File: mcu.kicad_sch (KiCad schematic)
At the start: 29 parts, among them J1 SM03B-SRSS-TB, SW1 SW_Push, SW2 SW_Push, U1 RP2350_60QFN, U2 W25Q128JVS, Y1 ABM8-272-T3

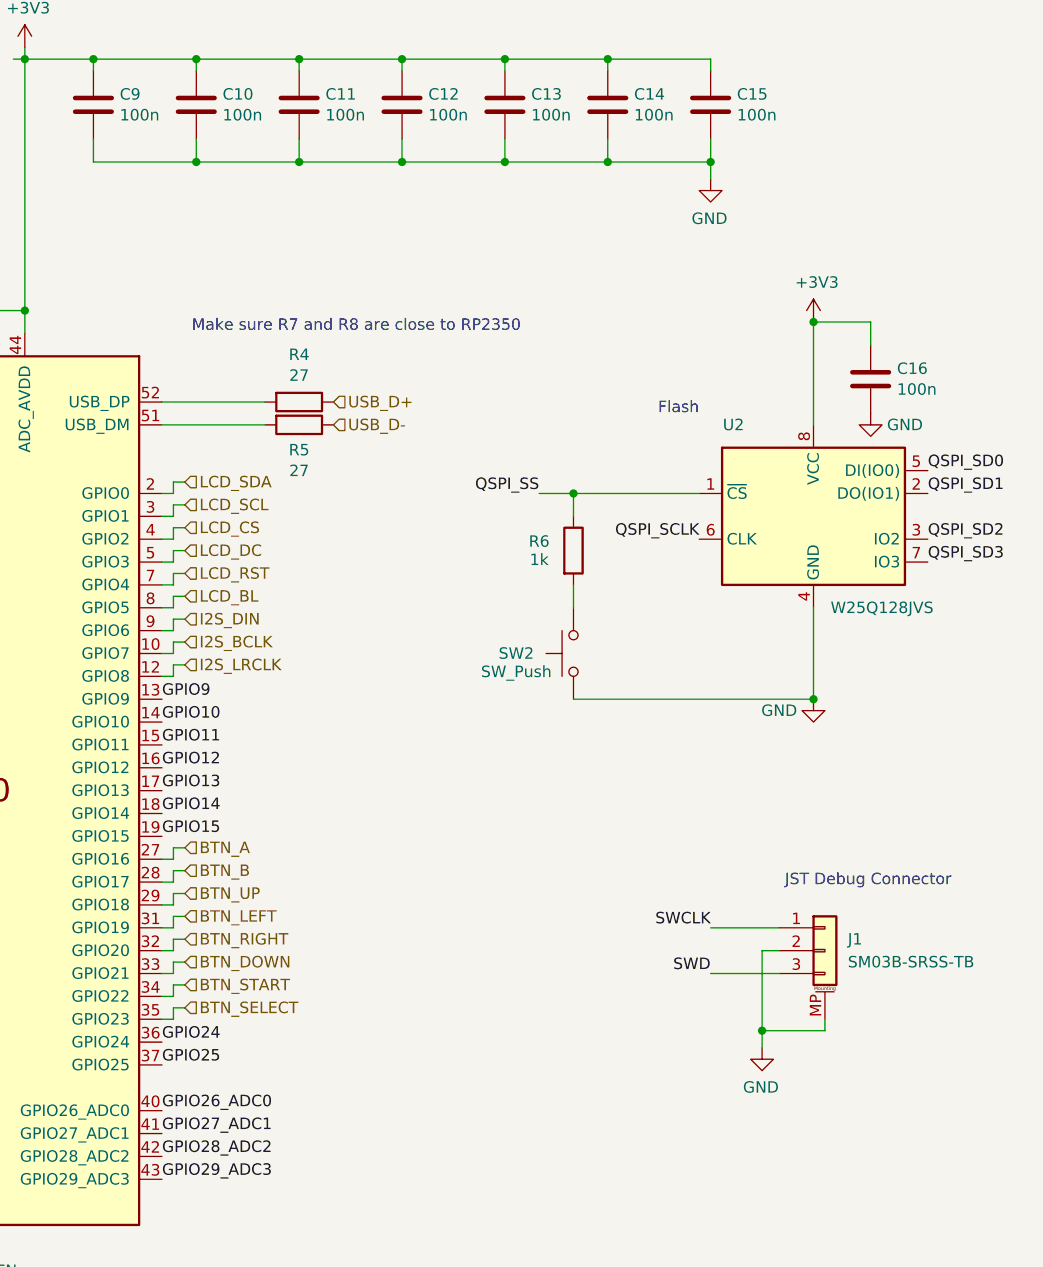
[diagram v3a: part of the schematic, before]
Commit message: add amplifier mode selector, add drawing lcd
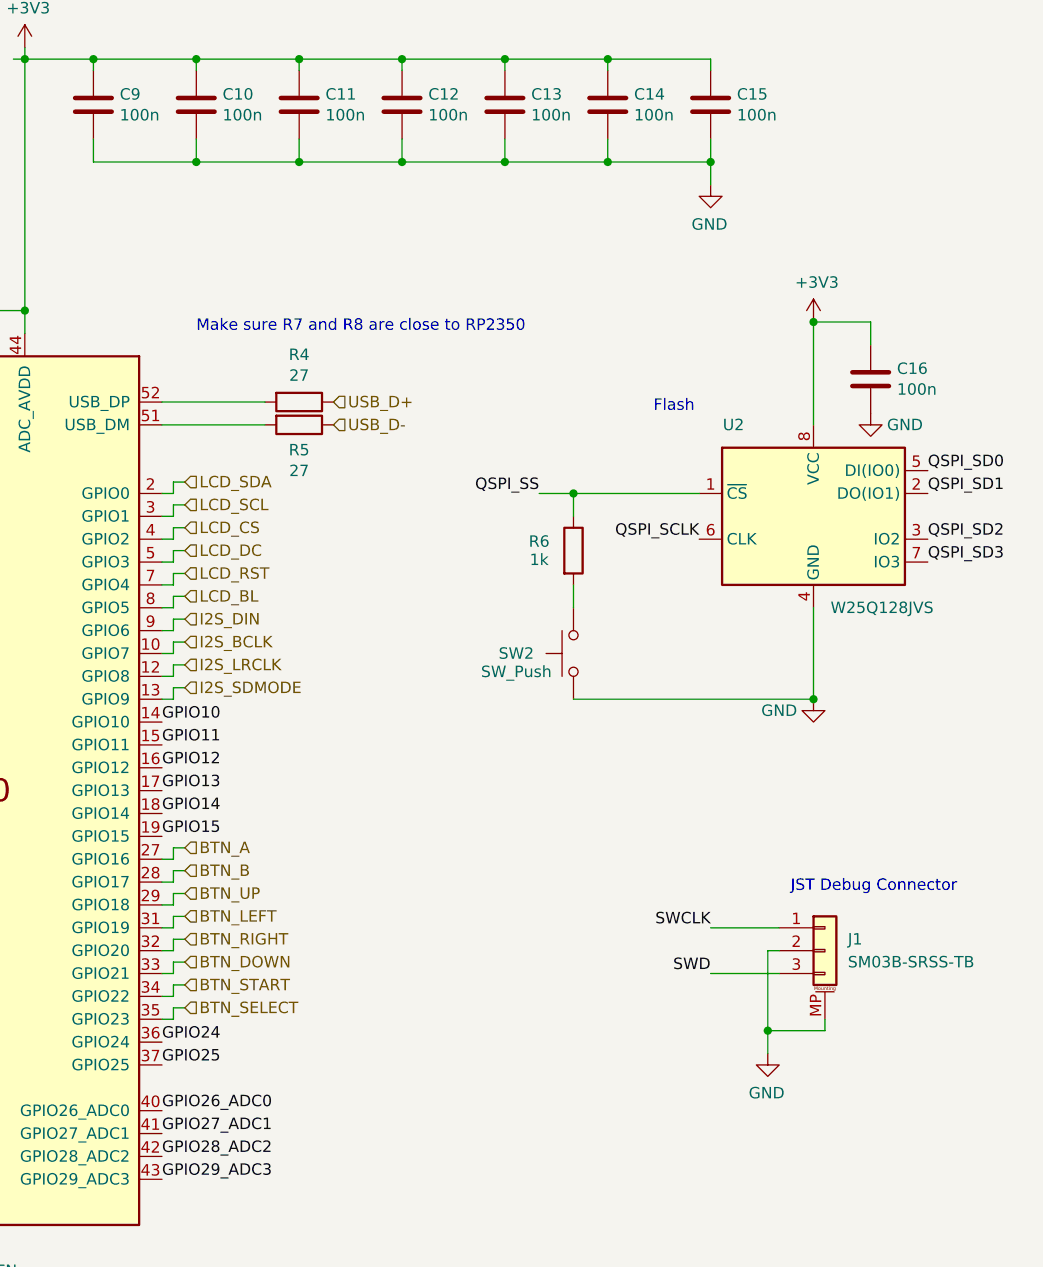
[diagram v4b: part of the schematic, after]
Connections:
- net GPIO9 renamed I2S_SDMODE
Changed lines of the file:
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@@
 	(text "Make sure R7 and R8 are close to RP2350\n"
 		(exclude_from_sim no)
-		(at 178.562 60.96 0)
+		(at 179.07 60.96 0)
 		(effects
 			(font
@@
 	(text "Flash"
 		(exclude_from_sim no)
-		(at 230.378 70.104 0)
+		(at 229.87 69.85 0)
 		(effects
 			(font
@@
 	(text "JST Debug Connector"
 		(exclude_from_sim no)
-		(at 244.475 122.555 0)
+		(at 245.11 123.19 0)
 		(effects
 			(font
@@
 	)
 	(junction
-		(at 241.935 138.43)
+		(at 242.57 138.43)
 		(diameter 0)
 		(color 0 0 0 0)
@@
 	(wire
 		(pts
-			(xy 236.22 41.91) (xy 236.22 43.815)
+			(xy 236.22 41.91) (xy 236.22 44.45)
 		)
 		(stroke
@@
 	(wire
 		(pts
+			(xy 176.53 101.6) (xy 175.26 101.6)
+		)
+		(stroke
+			(width 0)
+			(type default)
+		)
+	)
+	(wire
+		(pts
 			(xy 68.58 120.65) (xy 68.58 121.92)
 		)
@@
 	(wire
 		(pts
-			(xy 241.935 138.43) (xy 241.935 140.335)
+			(xy 176.53 100.33) (xy 176.53 101.6)
+		)
+		(stroke
+			(width 0)
+			(type default)
+		)
+	)
+	(wire
+		(pts
+			(xy 242.57 138.43) (xy 242.57 140.97)
 		)
 		(stroke
@@
 	(wire
 		(pts
-			(xy 241.935 138.43) (xy 248.92 138.43)
+			(xy 242.57 138.43) (xy 248.92 138.43)
 		)
 		(stroke
@@
 	(wire
 		(pts
+			(xy 176.53 100.33) (xy 177.8 100.33)
+		)
+		(stroke
+			(width 0)
+			(type default)
+		)
+	)
+	(wire
+		(pts
 			(xy 46.99 121.92) (xy 46.99 124.46)
 		)
@@
 	(wire
 		(pts
-			(xy 243.84 129.54) (xy 241.935 129.54)
+			(xy 243.84 129.54) (xy 242.57 129.54)
 		)
 		(stroke
@@
 	(wire
 		(pts
-			(xy 241.935 129.54) (xy 241.935 138.43)
+			(xy 242.57 129.54) (xy 242.57 138.43)
 		)
 		(stroke
@@
 		)
 	)
-	(label "GPIO9"
-		(at 175.26 101.6 0)
-		(effects
-			(font
-				(size 1.27 1.27)
-			)
-			(justify left bottom)
-		)
-	)
 	(label "QSPI_SD3"
 		(at 111.76 101.6 180)
@@
 		)
 	)
+	(hierarchical_label "I2S_SDMODE"
+		(shape input)
+		(at 177.8 100.33 0)
+		(effects
+			(font
+				(size 1.27 1.27)
+			)
+			(justify left)
+		)
+	)
 	(hierarchical_label "BTN_START"
 		(shape input)
@@
 	(symbol
 		(lib_id "power:GND")
-		(at 241.935 140.335 0)
+		(at 242.57 140.97 0)
 		(mirror y)
 		(unit 1)
@@
 		(dnp no)
 		(property "Reference" "#PWR014"
-			(at 241.935 146.685 0)
+			(at 242.57 147.32 0)
 			(effects
 				(font
@@
 		)
 		(property "Value" "GND"
-			(at 241.808 144.7292 0)
+			(at 242.443 145.3642 0)
 			(effects
 				(font
@@
 		)
 		(property "Footprint" ""
-			(at 241.935 140.335 0)
+			(at 242.57 140.97 0)
 			(effects
 				(font
@@
 		)
 		(property "Datasheet" ""
-			(at 241.935 140.335 0)
+			(at 242.57 140.97 0)
 			(effects
 				(font
@@
 		)
 		(property "Description" ""
-			(at 241.935 140.335 0)
+			(at 242.57 140.97 0)
 			(effects
 				(font
@@
 	(symbol
 		(lib_id "power:GND")
-		(at 236.22 43.815 0)
+		(at 236.22 44.45 0)
 		(mirror y)
 		(unit 1)
@@
 		(dnp no)
 		(property "Reference" "#PWR013"
-			(at 236.22 50.165 0)
+			(at 236.22 50.8 0)
 			(effects
 				(font
@@
 		)
 		(property "Value" "GND"
-			(at 236.093 48.2092 0)
+			(at 236.093 48.8442 0)
 			(effects
 				(font
@@
 		)
 		(property "Footprint" ""
-			(at 236.22 43.815 0)
+			(at 236.22 44.45 0)
 			(effects
 				(font
@@
 		)
 		(property "Datasheet" ""
-			(at 236.22 43.815 0)
+			(at 236.22 44.45 0)
 			(effects
 				(font
@@
 		)
 		(property "Description" ""
-			(at 236.22 43.815 0)
+			(at 236.22 44.45 0)
 			(effects
 				(font

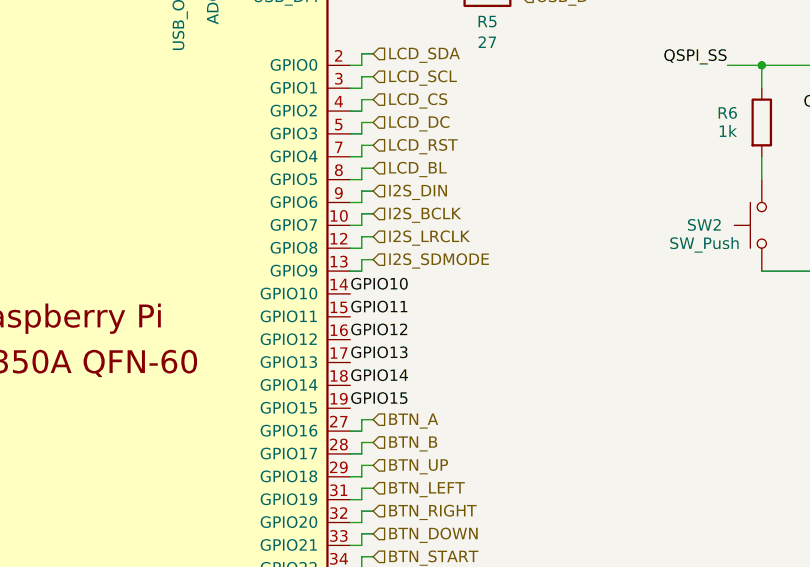
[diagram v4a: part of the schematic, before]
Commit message: add vibration motor
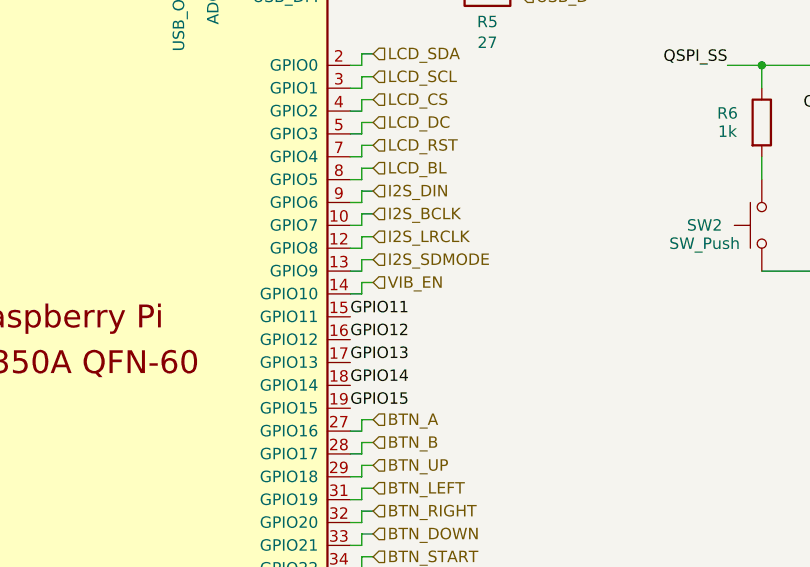
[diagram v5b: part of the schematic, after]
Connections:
- net GPIO10 renamed VIB_EN
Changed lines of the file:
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@@
+	(wire
+		(pts
+			(xy 176.53 104.14) (xy 175.26 104.14)
+		)
+		(stroke
+			(width 0)
+			(type default)
+		)
+	)
 	(wire
 		(pts
@@
 	(wire
 		(pts
+			(xy 176.53 102.87) (xy 176.53 104.14)
+		)
+		(stroke
+			(width 0)
+			(type default)
+		)
+	)
+	(wire
+		(pts
 			(xy 176.53 97.79) (xy 176.53 99.06)
 		)
@@
 		(pts
 			(xy 106.68 72.39) (xy 111.76 72.39)
+		)
+		(stroke
+			(width 0)
+			(type default)
+		)
+	)
+	(wire
+		(pts
+			(xy 176.53 102.87) (xy 177.8 102.87)
 		)
 		(stroke
@@
 	(label "GPIO24"
 		(at 175.26 139.7 0)
-		(effects
-			(font
-				(size 1.27 1.27)
-			)
-			(justify left bottom)
-		)
-	)
-	(label "GPIO10"
-		(at 175.26 104.14 0)
 		(effects
 			(font
@@
 		(effects
 			(font
+				(size 1.27 1.27)
+			)
+			(justify left)
+		)
+	)
+	(hierarchical_label "VIB_EN"
+		(shape input)
+		(at 177.8 102.87 0)
+		(effects
+			(font

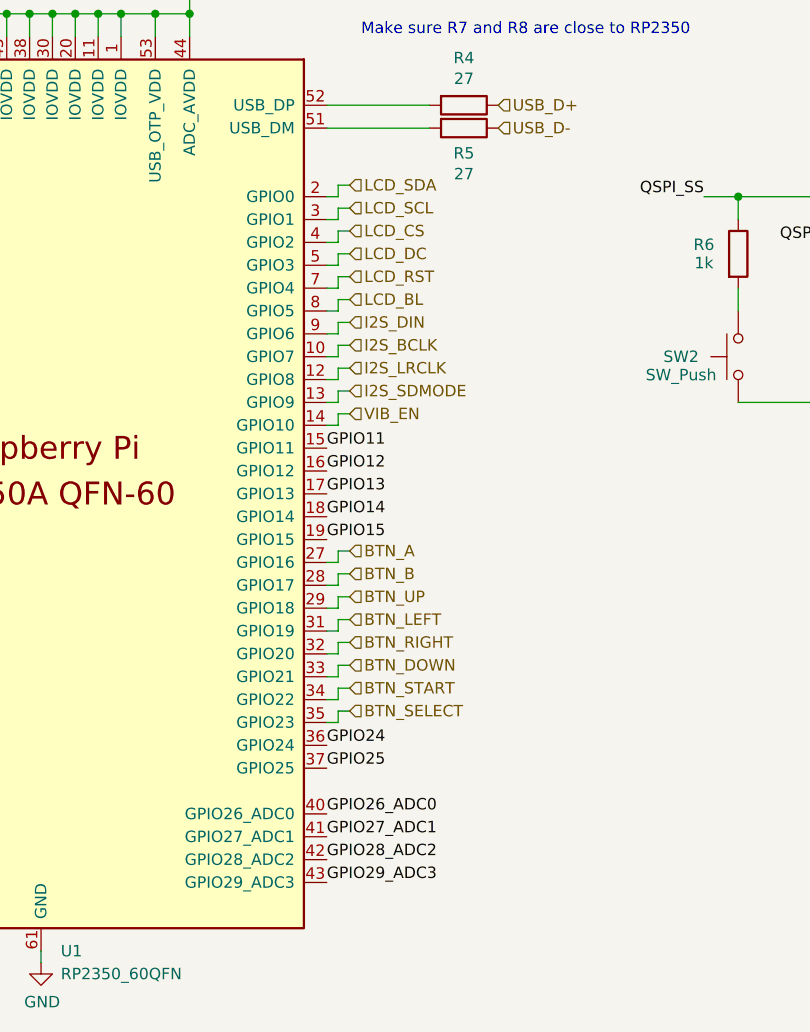
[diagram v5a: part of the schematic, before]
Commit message: add SD card
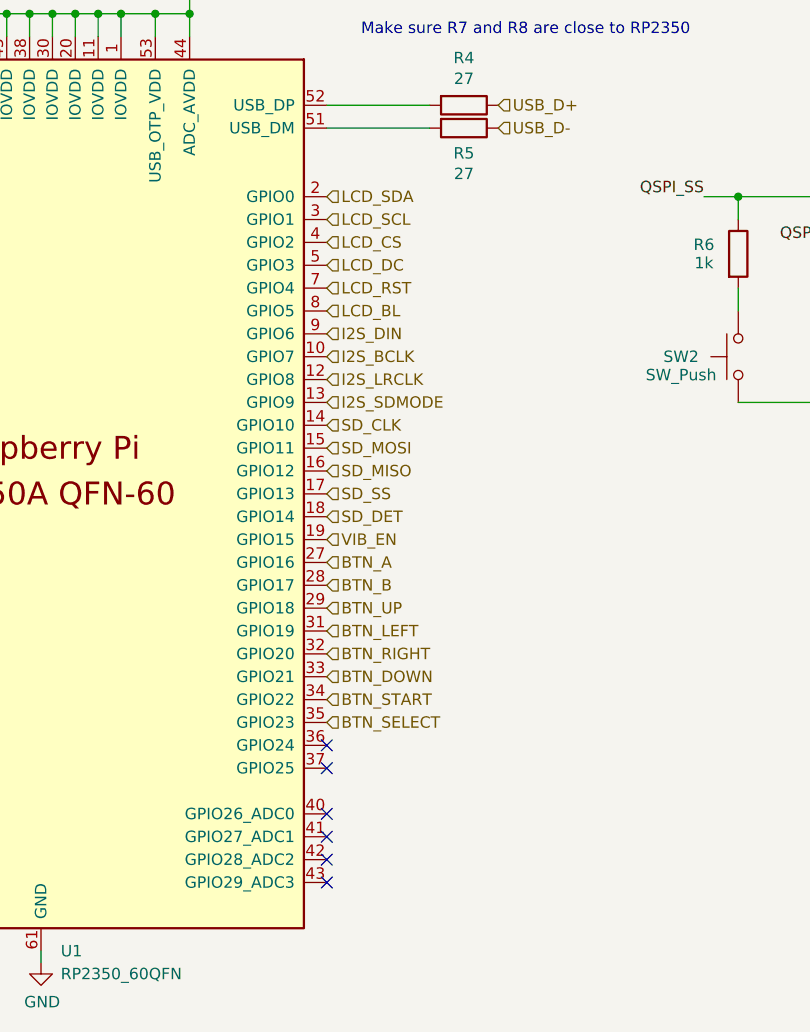
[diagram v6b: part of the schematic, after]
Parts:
- U2: footprint RP2350_60QFN_minimal:Crystal_SMD_HC49-US -> Package_SO:SOIC-8_5.3x5.3mm_P1.27mm
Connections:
- net GPIO15 is gone; now on net VIB_EN: U1.19 (GPIO15)
- net VIB_EN: no longer U1.14 (GPIO10)
- net GPIO11 renamed SD_MOSI
- net GPIO12 renamed SD_MISO
- net GPIO13 renamed SD_SS
- net GPIO14 renamed SD_DET
- net GPIO24: no longer names the net of U1.36 (GPIO24)
- net GPIO25: no longer names the net of U1.37 (GPIO25)
- net GPIO26_ADC0: no longer names the net of U1.40 (GPIO26_ADC0)
- net GPIO27_ADC1: no longer names the net of U1.41 (GPIO27_ADC1)
- net GPIO28_ADC2: no longer names the net of U1.42 (GPIO28_ADC2)
- net GPIO29_ADC3: no longer names the net of U1.43 (GPIO29_ADC3)
- new net SD_CLK: U1.14 (GPIO10)
- no-connect marks 0 -> 6
